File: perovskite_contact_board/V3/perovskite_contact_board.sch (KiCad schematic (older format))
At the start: 31 parts, among them U1 Perovskite_CP_6_Cell, U2 Perovskite_CP_6_Cell, U3 Perovskite_CP_6_Cell, U4 MCP9808_MSOP, U5 MCP9808_MSOP, U6 MCP9808_MSOP

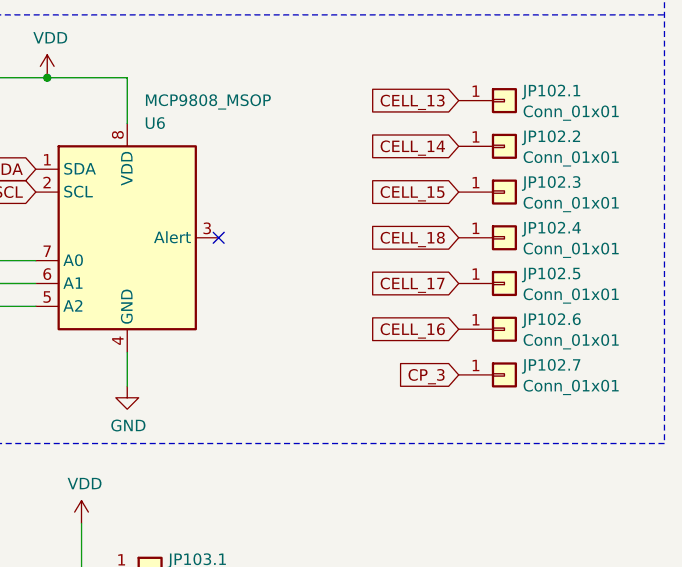
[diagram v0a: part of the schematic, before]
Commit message: Update ready for review
Swapped to circular 2mm touch point pads.
Updated 3d models.
Ready for review.
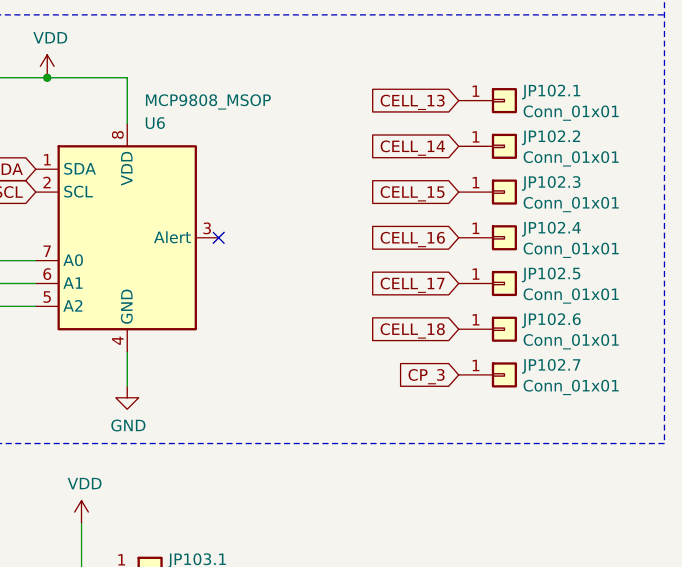
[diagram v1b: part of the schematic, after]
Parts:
- JP100.1, JP100.2, JP100.3, JP100.4, JP100.5, JP100.6, JP100.7, JP101.1, JP101.2, JP101.3, JP101.4, JP101.5, JP101.6, JP101.7, JP102.1, JP102.2, JP102.3, JP102.4, JP102.5, JP102.6, JP102.7, JP103.1, JP103.2, JP103.3, JP103.4: footprint TestPoint:TestPoint_Keystone_5015_Micro-Minature -> TestPoint:TestPoint_Pad_D2.0mm
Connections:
- net CELL_16: now also JP102.4.1 (Pin_1); no longer JP102.6.1 (Pin_1)
- net CELL_18: now also JP102.6.1 (Pin_1); no longer JP102.4.1 (Pin_1)
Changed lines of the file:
@@
 Text GLabel 7000 4050 0    50   Input ~ 0
 CELL_12
-Text GLabel 6950 5900 0    50   Input ~ 0
+Text GLabel 6950 5500 0    50   Input ~ 0
 CELL_16
 $Comp
@@
 F 0 "JP100.1" H 7280 1192 50  0000 L CNN
 F 1 "Conn_01x01" H 7280 1101 50  0000 L CNN
-F 2 "TestPoint:TestPoint_Keystone_5015_Micro-Minature" H 7200 1150 50  0001 C CNN
+F 2 "TestPoint:TestPoint_Pad_D2.0mm" H 7200 1150 50  0001 C CNN
 F 3 "~" H 7200 1150 50  0001 C CNN
 	1    7200 1150
@@
 F 0 "JP100.2" H 7280 1392 50  0000 L CNN
 F 1 "Conn_01x01" H 7280 1301 50  0000 L CNN
-F 2 "TestPoint:TestPoint_Keystone_5015_Micro-Minature" H 7200 1350 50  0001 C CNN
+F 2 "TestPoint:TestPoint_Pad_D2.0mm" H 7200 1350 50  0001 C CNN
 F 3 "~" H 7200 1350 50  0001 C CNN
 	1    7200 1350
@@
 F 0 "JP100.3" H 7280 1592 50  0000 L CNN
 F 1 "Conn_01x01" H 7280 1501 50  0000 L CNN
-F 2 "TestPoint:TestPoint_Keystone_5015_Micro-Minature" H 7200 1550 50  0001 C CNN
+F 2 "TestPoint:TestPoint_Pad_D2.0mm" H 7200 1550 50  0001 C CNN
 F 3 "~" H 7200 1550 50  0001 C CNN
 	1    7200 1550
@@
 F 0 "JP100.4" H 7280 1792 50  0000 L CNN
 F 1 "Conn_01x01" H 7280 1701 50  0000 L CNN
-F 2 "TestPoint:TestPoint_Keystone_5015_Micro-Minature" H 7200 1750 50  0001 C CNN
+F 2 "TestPoint:TestPoint_Pad_D2.0mm" H 7200 1750 50  0001 C CNN
 F 3 "~" H 7200 1750 50  0001 C CNN
 	1    7200 1750
@@
 F 0 "JP100.5" H 7280 1992 50  0000 L CNN
 F 1 "Conn_01x01" H 7280 1901 50  0000 L CNN
-F 2 "TestPoint:TestPoint_Keystone_5015_Micro-Minature" H 7200 1950 50  0001 C CNN
+F 2 "TestPoint:TestPoint_Pad_D2.0mm" H 7200 1950 50  0001 C CNN
 F 3 "~" H 7200 1950 50  0001 C CNN
 	1    7200 1950
@@
 F 0 "JP100.6" H 7280 2192 50  0000 L CNN
 F 1 "Conn_01x01" H 7280 2101 50  0000 L CNN
-F 2 "TestPoint:TestPoint_Keystone_5015_Micro-Minature" H 7200 2150 50  0001 C CNN
+F 2 "TestPoint:TestPoint_Pad_D2.0mm" H 7200 2150 50  0001 C CNN
 F 3 "~" H 7200 2150 50  0001 C CNN
 	1    7200 2150
@@
 F 0 "JP100.7" H 7280 2392 50  0000 L CNN
 F 1 "Conn_01x01" H 7280 2301 50  0000 L CNN
-F 2 "TestPoint:TestPoint_Keystone_5015_Micro-Minature" H 7200 2350 50  0001 C CNN
+F 2 "TestPoint:TestPoint_Pad_D2.0mm" H 7200 2350 50  0001 C CNN
 F 3 "~" H 7200 2350 50  0001 C CNN
 	1    7200 2350
@@
 F 0 "JP101.1" H 7280 3092 50  0000 L CNN
 F 1 "Conn_01x01" H 7280 3001 50  0000 L CNN
-F 2 "TestPoint:TestPoint_Keystone_5015_Micro-Minature" H 7200 3050 50  0001 C CNN
+F 2 "TestPoint:TestPoint_Pad_D2.0mm" H 7200 3050 50  0001 C CNN
 F 3 "~" H 7200 3050 50  0001 C CNN
 	1    7200 3050
@@
 F 0 "JP101.2" H 7280 3292 50  0000 L CNN
 F 1 "Conn_01x01" H 7280 3201 50  0000 L CNN
-F 2 "TestPoint:TestPoint_Keystone_5015_Micro-Minature" H 7200 3250 50  0001 C CNN
+F 2 "TestPoint:TestPoint_Pad_D2.0mm" H 7200 3250 50  0001 C CNN
 F 3 "~" H 7200 3250 50  0001 C CNN
 	1    7200 3250
@@
 F 0 "JP101.3" H 7280 3492 50  0000 L CNN
 F 1 "Conn_01x01" H 7280 3401 50  0000 L CNN
-F 2 "TestPoint:TestPoint_Keystone_5015_Micro-Minature" H 7200 3450 50  0001 C CNN
+F 2 "TestPoint:TestPoint_Pad_D2.0mm" H 7200 3450 50  0001 C CNN
 F 3 "~" H 7200 3450 50  0001 C CNN
 	1    7200 3450
@@
 F 0 "JP101.4" H 7280 3692 50  0000 L CNN
 F 1 "Conn_01x01" H 7280 3601 50  0000 L CNN
-F 2 "TestPoint:TestPoint_Keystone_5015_Micro-Minature" H 7200 3650 50  0001 C CNN
+F 2 "TestPoint:TestPoint_Pad_D2.0mm" H 7200 3650 50  0001 C CNN
 F 3 "~" H 7200 3650 50  0001 C CNN
 	1    7200 3650
@@
 F 0 "JP101.5" H 7280 3892 50  0000 L CNN
 F 1 "Conn_01x01" H 7280 3801 50  0000 L CNN
-F 2 "TestPoint:TestPoint_Keystone_5015_Micro-Minature" H 7200 3850 50  0001 C CNN
+F 2 "TestPoint:TestPoint_Pad_D2.0mm" H 7200 3850 50  0001 C CNN
 F 3 "~" H 7200 3850 50  0001 C CNN
 	1    7200 3850
@@
 F 0 "JP101.6" H 7280 4092 50  0000 L CNN
 F 1 "Conn_01x01" H 7280 4001 50  0000 L CNN
-F 2 "TestPoint:TestPoint_Keystone_5015_Micro-Minature" H 7200 4050 50  0001 C CNN
+F 2 "TestPoint:TestPoint_Pad_D2.0mm" H 7200 4050 50  0001 C CNN
 F 3 "~" H 7200 4050 50  0001 C CNN
 	1    7200 4050
@@
 F 0 "JP101.7" H 7280 4292 50  0000 L CNN
 F 1 "Conn_01x01" H 7280 4201 50  0000 L CNN
-F 2 "TestPoint:TestPoint_Keystone_5015_Micro-Minature" H 7200 4250 50  0001 C CNN
+F 2 "TestPoint:TestPoint_Pad_D2.0mm" H 7200 4250 50  0001 C CNN
 F 3 "~" H 7200 4250 50  0001 C CNN
 	1    7200 4250
@@
 F 0 "JP102.1" H 7230 4942 50  0000 L CNN
 F 1 "Conn_01x01" H 7230 4851 50  0000 L CNN
-F 2 "TestPoint:TestPoint_Keystone_5015_Micro-Minature" H 7150 4900 50  0001 C CNN
+F 2 "TestPoint:TestPoint_Pad_D2.0mm" H 7150 4900 50  0001 C CNN
 F 3 "~" H 7150 4900 50  0001 C CNN
 	1    7150 4900
@@
 F 0 "JP102.2" H 7230 5142 50  0000 L CNN
 F 1 "Conn_01x01" H 7230 5051 50  0000 L CNN
-F 2 "TestPoint:TestPoint_Keystone_5015_Micro-Minature" H 7150 5100 50  0001 C CNN
+F 2 "TestPoint:TestPoint_Pad_D2.0mm" H 7150 5100 50  0001 C CNN
 F 3 "~" H 7150 5100 50  0001 C CNN
 	1    7150 5100
@@
 F 0 "JP102.3" H 7230 5342 50  0000 L CNN
 F 1 "Conn_01x01" H 7230 5251 50  0000 L CNN
-F 2 "TestPoint:TestPoint_Keystone_5015_Micro-Minature" H 7150 5300 50  0001 C CNN
+F 2 "TestPoint:TestPoint_Pad_D2.0mm" H 7150 5300 50  0001 C CNN
 F 3 "~" H 7150 5300 50  0001 C CNN
 	1    7150 5300
@@
 F 0 "JP102.4" H 7230 5542 50  0000 L CNN
 F 1 "Conn_01x01" H 7230 5451 50  0000 L CNN
-F 2 "TestPoint:TestPoint_Keystone_5015_Micro-Minature" H 7150 5500 50  0001 C CNN
+F 2 "TestPoint:TestPoint_Pad_D2.0mm" H 7150 5500 50  0001 C CNN
 F 3 "~" H 7150 5500 50  0001 C CNN
 	1    7150 5500
@@
 F 0 "JP102.5" H 7230 5742 50  0000 L CNN
 F 1 "Conn_01x01" H 7230 5651 50  0000 L CNN
-F 2 "TestPoint:TestPoint_Keystone_5015_Micro-Minature" H 7150 5700 50  0001 C CNN
+F 2 "TestPoint:TestPoint_Pad_D2.0mm" H 7150 5700 50  0001 C CNN
 F 3 "~" H 7150 5700 50  0001 C CNN
 	1    7150 5700
@@
 F 0 "JP102.6" H 7230 5942 50  0000 L CNN
 F 1 "Conn_01x01" H 7230 5851 50  0000 L CNN
-F 2 "TestPoint:TestPoint_Keystone_5015_Micro-Minature" H 7150 5900 50  0001 C CNN
+F 2 "TestPoint:TestPoint_Pad_D2.0mm" H 7150 5900 50  0001 C CNN
 F 3 "~" H 7150 5900 50  0001 C CNN
 	1    7150 5900
@@
 F 0 "JP102.7" H 7230 6142 50  0000 L CNN
 F 1 "Conn_01x01" H 7230 6051 50  0000 L CNN
-F 2 "TestPoint:TestPoint_Keystone_5015_Micro-Minature" H 7150 6100 50  0001 C CNN
+F 2 "TestPoint:TestPoint_Pad_D2.0mm" H 7150 6100 50  0001 C CNN
 F 3 "~" H 7150 6100 50  0001 C CNN
 	1    7150 6100
@@
 F 0 "JP103.1" H 5680 6992 50  0000 L CNN
 F 1 "Conn_01x01" H 5680 6901 50  0000 L CNN
-F 2 "TestPoint:TestPoint_Keystone_5015_Micro-Minature" H 5600 6950 50  0001 C CNN
+F 2 "TestPoint:TestPoint_Pad_D2.0mm" H 5600 6950 50  0001 C CNN
 F 3 "~" H 5600 6950 50  0001 C CNN
 	1    5600 6950
@@
 F 0 "JP103.2" H 5680 7192 50  0000 L CNN
 F 1 "Conn_01x01" H 5680 7101 50  0000 L CNN
-F 2 "TestPoint:TestPoint_Keystone_5015_Micro-Minature" H 5600 7150 50  0001 C CNN
+F 2 "TestPoint:TestPoint_Pad_D2.0mm" H 5600 7150 50  0001 C CNN
 F 3 "~" H 5600 7150 50  0001 C CNN
 	1    5600 7150
@@
 F 0 "JP103.3" H 5680 7392 50  0000 L CNN
 F 1 "Conn_01x01" H 5680 7301 50  0000 L CNN
-F 2 "TestPoint:TestPoint_Keystone_5015_Micro-Minature" H 5600 7350 50  0001 C CNN
+F 2 "TestPoint:TestPoint_Pad_D2.0mm" H 5600 7350 50  0001 C CNN
 F 3 "~" H 5600 7350 50  0001 C CNN
 	1    5600 7350
@@
 F 0 "JP103.4" H 5680 7592 50  0000 L CNN
 F 1 "Conn_01x01" H 5680 7501 50  0000 L CNN
-F 2 "TestPoint:TestPoint_Keystone_5015_Micro-Minature" H 5600 7550 50  0001 C CNN
+F 2 "TestPoint:TestPoint_Pad_D2.0mm" H 5600 7550 50  0001 C CNN
 F 3 "~" H 5600 7550 50  0001 C CNN
 	1    5600 7550
@@
 $EndComp
 $Comp
-L power:GND #PWR?
+L power:GND #PWR0102
 U 1 1 64BAB42F
 P 5050 7300
-F 0 "#PWR?" H 5050 7050 50  0001 C CNN
+F 0 "#PWR0102" H 5050 7050 50  0001 C CNN
 F 1 "GND" H 5055 7127 50  0000 C CNN
 F 2 "" H 5050 7300 50  0001 C CNN
@@
 	5050 6950 5050 7300
 $Comp
-L power:VDD #PWR?
+L power:VDD #PWR0103
 U 1 1 64BB3055
 P 5300 6750
-F 0 "#PWR?" H 5300 6600 50  0001 C CNN
+F 0 "#PWR0103" H 5300 6600 50  0001 C CNN
 F 1 "VDD" H 5315 6923 50  0000 C CNN
 F 2 "" H 5300 6750 50  0001 C CNN
@@
 	7850 2675 975  2675
 $Comp
-L power:VDD #PWR?
+L power:VDD #PWR0105
 U 1 1 64BC9726
 P 5150 4800
-F 0 "#PWR?" H 5150 4650 50  0001 C CNN
+F 0 "#PWR0105" H 5150 4650 50  0001 C CNN
 F 1 "VDD" H 5165 4973 50  0000 C CNN
 F 2 "" H 5150 4800 50  0001 C CNN
@@
 	5150 4800 4800 4800
 $Comp
-L power:VDD #PWR?
+L power:VDD #PWR0106
 U 1 1 64BCA3BE
 P 5150 2950
-F 0 "#PWR?" H 5150 2800 50  0001 C CNN
+F 0 "#PWR0106" H 5150 2800 50  0001 C CNN
 F 1 "VDD" H 5165 3123 50  0000 C CNN
 F 2 "" H 5150 2950 50  0001 C CNN
@@
 	5150 2950 4750 2950
 $Comp
-L power:VDD #PWR?
+L power:VDD #PWR0107
 U 1 1 64BCB08F
 P 5150 1200
-F 0 "#PWR?" H 5150 1050 50  0001 C CNN
+F 0 "#PWR0107" H 5150 1050 50  0001 C CNN
 F 1 "VDD" H 5165 1373 50  0000 C CNN
 F 2 "" H 5150 1200 50  0001 C CNN
@@
 Wire Wire Line
 	5150 1200 4800 1200
-Text GLabel 6950 5500 0    50   Input ~ 0
+Text GLabel 6950 5900 0    50   Input ~ 0
 CELL_18
 Text GLabel 6950 5700 0    50   Input ~ 0

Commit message: Review contact board
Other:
- moved on the sheet: JP100.1, JP100.2, JP100.3, JP100.4, JP100.5, JP100.6, JP100.7, JP101.1, JP101.2, JP101.3, JP101.4, JP101.5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

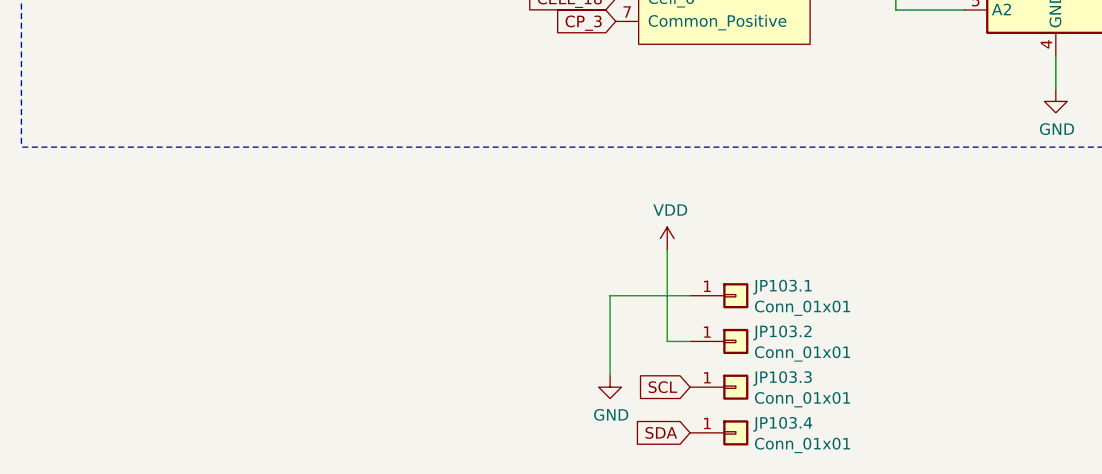
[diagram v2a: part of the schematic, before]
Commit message: centered vias, added all redundant pads, standardized text
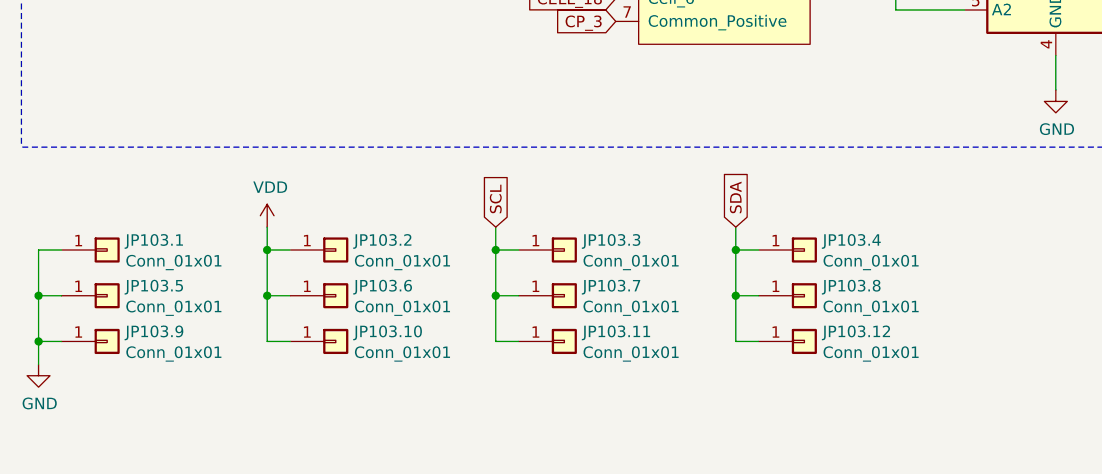
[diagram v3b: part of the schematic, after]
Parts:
- added JP103.10, JP103.11, JP103.12, JP103.5, JP103.6, JP103.7, JP103.8, JP103.9: Conn_01x01, TestPoint:TestPoint_Pad_D2.0mm, symbol Connector_Generic:Conn_01x01
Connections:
- net GND: now also JP103.5.1 (Pin_1), JP103.9.1 (Pin_1)
- net SCL: now also JP103.11.1 (Pin_1), JP103.7.1 (Pin_1)
- net SDA: now also JP103.12.1 (Pin_1), JP103.8.1 (Pin_1)
- net VDD: now also JP103.10.1 (Pin_1), JP103.6.1 (Pin_1)
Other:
- moved on the sheet: JP103.1, JP103.2, JP103.3, JP103.4
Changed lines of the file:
@@
 Sheet 1 1
 Title "Perovskite Contact Board"
-Date "2022-11-26"
-Rev "Version 1"
+Date "2023-07-20"
+Rev "V3"
 Comp "Aerospace eXperimental Payloads | UNL Aerospace Club"
 Comment1 "Copyright (c) 2022"
@@
 L Connector_Generic:Conn_01x01 JP103.1
 U 1 1 64B5D0FC
-P 5600 6950
-F 0 "JP103.1" H 5680 6992 50  0000 L CNN
-F 1 "Conn_01x01" H 5680 6901 50  0000 L CNN
-F 2 "TestPoint:TestPoint_Pad_D2.0mm" H 5600 6950 50  0001 C CNN
-F 3 "~" H 5600 6950 50  0001 C CNN
-	1    5600 6950
+P 2850 6750
+F 0 "JP103.1" H 2930 6792 50  0000 L CNN
+F 1 "Conn_01x01" H 2930 6701 50  0000 L CNN
+F 2 "TestPoint:TestPoint_Pad_D2.0mm" H 2850 6750 50  0001 C CNN
+F 3 "~" H 2850 6750 50  0001 C CNN
+	1    2850 6750
 	1    0    0    -1
 $EndComp
@@
 L Connector_Generic:Conn_01x01 JP103.2
 U 1 1 64B5D102
-P 5600 7150
-F 0 "JP103.2" H 5680 7192 50  0000 L CNN
-F 1 "Conn_01x01" H 5680 7101 50  0000 L CNN
-F 2 "TestPoint:TestPoint_Pad_D2.0mm" H 5600 7150 50  0001 C CNN
-F 3 "~" H 5600 7150 50  0001 C CNN
-	1    5600 7150
+P 3850 6750
+F 0 "JP103.2" H 3930 6792 50  0000 L CNN
+F 1 "Conn_01x01" H 3930 6701 50  0000 L CNN
+F 2 "TestPoint:TestPoint_Pad_D2.0mm" H 3850 6750 50  0001 C CNN
+F 3 "~" H 3850 6750 50  0001 C CNN
+	1    3850 6750
 	1    0    0    -1
 $EndComp
@@
 L Connector_Generic:Conn_01x01 JP103.3
 U 1 1 64B5D108
-P 5600 7350
-F 0 "JP103.3" H 5680 7392 50  0000 L CNN
-F 1 "Conn_01x01" H 5680 7301 50  0000 L CNN
-F 2 "TestPoint:TestPoint_Pad_D2.0mm" H 5600 7350 50  0001 C CNN
-F 3 "~" H 5600 7350 50  0001 C CNN
-	1    5600 7350
+P 4850 6750
+F 0 "JP103.3" H 4930 6792 50  0000 L CNN
+F 1 "Conn_01x01" H 4930 6701 50  0000 L CNN
+F 2 "TestPoint:TestPoint_Pad_D2.0mm" H 4850 6750 50  0001 C CNN
+F 3 "~" H 4850 6750 50  0001 C CNN
+	1    4850 6750
 	1    0    0    -1
 $EndComp
@@
 L Connector_Generic:Conn_01x01 JP103.4
 U 1 1 64B7D4E1
-P 5600 7550
-F 0 "JP103.4" H 5680 7592 50  0000 L CNN
-F 1 "Conn_01x01" H 5680 7501 50  0000 L CNN
-F 2 "TestPoint:TestPoint_Pad_D2.0mm" H 5600 7550 50  0001 C CNN
-F 3 "~" H 5600 7550 50  0001 C CNN
-	1    5600 7550
+P 5900 6750
+F 0 "JP103.4" H 5980 6792 50  0000 L CNN
+F 1 "Conn_01x01" H 5980 6701 50  0000 L CNN
+F 2 "TestPoint:TestPoint_Pad_D2.0mm" H 5900 6750 50  0001 C CNN
+F 3 "~" H 5900 6750 50  0001 C CNN
+	1    5900 6750
 	1    0    0    -1
 $EndComp
@@
 L power:GND #PWR0102
 U 1 1 64BAB42F
-P 5050 7300
-F 0 "#PWR0102" H 5050 7050 50  0001 C CNN
-F 1 "GND" H 5055 7127 50  0000 C CNN
-F 2 "" H 5050 7300 50  0001 C CNN
-F 3 "" H 5050 7300 50  0001 C CNN
-	1    5050 7300
-	1    0    0    -1
-$EndComp
-Text GLabel 5400 7550 0    50   Input ~ 0
+P 2550 7250
+F 0 "#PWR0102" H 2550 7000 50  0001 C CNN
+F 1 "GND" H 2555 7077 50  0000 C CNN
+F 2 "" H 2550 7250 50  0001 C CNN
+F 3 "" H 2550 7250 50  0001 C CNN
+	1    2550 7250
+	1    0    0    -1
+$EndComp
+Text GLabel 5600 6650 1    50   Input ~ 0
 SDA
-Text GLabel 5400 7350 0    50   Input ~ 0
+Text GLabel 4550 6650 1    50   Input ~ 0
 SCL
-Wire Wire Line
-	5400 6950 5050 6950
-Wire Wire Line
-	5050 6950 5050 7300
 $Comp
 L power:VDD #PWR0103
 U 1 1 64BB3055
-P 5300 6750
-F 0 "#PWR0103" H 5300 6600 50  0001 C CNN
-F 1 "VDD" H 5315 6923 50  0000 C CNN
-F 2 "" H 5300 6750 50  0001 C CNN
-F 3 "" H 5300 6750 50  0001 C CNN
-	1    5300 6750
-	1    0    0    -1
-$EndComp
-Wire Wire Line
-	5400 7150 5300 7150
-Wire Wire Line
-	5300 7150 5300 6750
+P 3550 6650
+F 0 "#PWR0103" H 3550 6500 50  0001 C CNN
+F 1 "VDD" H 3565 6823 50  0000 C CNN
+F 2 "" H 3550 6650 50  0001 C CNN
+F 3 "" H 3550 6650 50  0001 C CNN
+	1    3550 6650
+	1    0    0    -1
+$EndComp
 NoConn ~ 7400 5400
 NoConn ~ 7400 3550
@@
 Text GLabel 8500 2250 0    50   Input ~ 0
 CP_1
+$Comp
+L Connector_Generic:Conn_01x01 JP103.5
+U 1 1 64B97803
+P 2850 6950
+F 0 "JP103.5" H 2930 6992 50  0000 L CNN
+F 1 "Conn_01x01" H 2930 6901 50  0000 L CNN
+F 2 "TestPoint:TestPoint_Pad_D2.0mm" H 2850 6950 50  0001 C CNN
+F 3 "~" H 2850 6950 50  0001 C CNN
+	1    2850 6950
+	1    0    0    -1
+$EndComp
+$Comp
+L Connector_Generic:Conn_01x01 JP103.9
+U 1 1 64B97AC2
+P 2850 7150
+F 0 "JP103.9" H 2930 7192 50  0000 L CNN
+F 1 "Conn_01x01" H 2930 7101 50  0000 L CNN
+F 2 "TestPoint:TestPoint_Pad_D2.0mm" H 2850 7150 50  0001 C CNN
+F 3 "~" H 2850 7150 50  0001 C CNN
+	1    2850 7150
+	1    0    0    -1
+$EndComp
+$Comp
+L Connector_Generic:Conn_01x01 JP103.6
+U 1 1 64B9861B
+P 3850 6950
+F 0 "JP103.6" H 3930 6992 50  0000 L CNN
+F 1 "Conn_01x01" H 3930 6901 50  0000 L CNN
+F 2 "TestPoint:TestPoint_Pad_D2.0mm" H 3850 6950 50  0001 C CNN
+F 3 "~" H 3850 6950 50  0001 C CNN
+	1    3850 6950
+	1    0    0    -1
+$EndComp
+$Comp
+L Connector_Generic:Conn_01x01 JP103.10
+U 1 1 64B988DA
+P 3850 7150
+F 0 "JP103.10" H 3930 7192 50  0000 L CNN
+F 1 "Conn_01x01" H 3930 7101 50  0000 L CNN
+F 2 "TestPoint:TestPoint_Pad_D2.0mm" H 3850 7150 50  0001 C CNN
+F 3 "~" H 3850 7150 50  0001 C CNN
+	1    3850 7150
+	1    0    0    -1
+$EndComp
+Wire Wire Line
+	3650 7150 3550 7150
+Wire Wire Line
+	3550 7150 3550 6950
+Wire Wire Line
+	3650 6750 3550 6750
+Connection ~ 3550 6750
+Wire Wire Line
+	3550 6750 3550 6650
+Wire Wire Line
+	3650 6950 3550 6950
+Connection ~ 3550 6950
+Wire Wire Line
+	3550 6950 3550 6750
+Wire Wire Line
+	2550 7250 2550 7150
+Wire Wire Line
+	2550 6750 2650 6750
+Wire Wire Line
+	2650 6950 2550 6950
+Connection ~ 2550 6950
+Wire Wire Line
+	2550 6950 2550 6750
+Wire Wire Line
+	2650 7150 2550 7150
+Connection ~ 2550 7150
+Wire Wire Line
+	2550 7150 2550 6950
+$Comp
+L Connector_Generic:Conn_01x01 JP103.7
+U 1 1 64BA556D
+P 4850 6950
+F 0 "JP103.7" H 4930 6992 50  0000 L CNN
+F 1 "Conn_01x01" H 4930 6901 50  0000 L CNN
+F 2 "TestPoint:TestPoint_Pad_D2.0mm" H 4850 6950 50  0001 C CNN
+F 3 "~" H 4850 6950 50  0001 C CNN
+	1    4850 6950
+	1    0    0    -1
+$EndComp
+$Comp
+L Connector_Generic:Conn_01x01 JP103.11
+U 1 1 64BA5848
+P 4850 7150
+F 0 "JP103.11" H 4930 7192 50  0000 L CNN
+F 1 "Conn_01x01" H 4930 7101 50  0000 L CNN
+F 2 "TestPoint:TestPoint_Pad_D2.0mm" H 4850 7150 50  0001 C CNN
+F 3 "~" H 4850 7150 50  0001 C CNN
+	1    4850 7150
+	1    0    0    -1
+$EndComp
+$Comp
+L Connector_Generic:Conn_01x01 JP103.8
+U 1 1 64BA5C01
+P 5900 6950
+F 0 "JP103.8" H 5980 6992 50  0000 L CNN
+F 1 "Conn_01x01" H 5980 6901 50  0000 L CNN
+F 2 "TestPoint:TestPoint_Pad_D2.0mm" H 5900 6950 50  0001 C CNN
+F 3 "~" H 5900 6950 50  0001 C CNN
+	1    5900 6950
+	1    0    0    -1
+$EndComp
+$Comp
+L Connector_Generic:Conn_01x01 JP103.12
+U 1 1 64BA5ED3
+P 5900 7150
+F 0 "JP103.12" H 5980 7192 50  0000 L CNN
+F 1 "Conn_01x01" H 5980 7101 50  0000 L CNN
+F 2 "TestPoint:TestPoint_Pad_D2.0mm" H 5900 7150 50  0001 C CNN
+F 3 "~" H 5900 7150 50  0001 C CNN
+	1    5900 7150
+	1    0    0    -1
+$EndComp
+Wire Wire Line
+	4550 6650 4550 6750
+Wire Wire Line
+	4550 7150 4650 7150
+Wire Wire Line
+	4650 6750 4550 6750
+Connection ~ 4550 6750
+Wire Wire Line
+	4550 6750 4550 6950
+Wire Wire Line
+	4650 6950 4550 6950
+Connection ~ 4550 6950
+Wire Wire Line
+	4550 6950 4550 7150
+Wire Wire Line
+	5600 6650 5600 6750
+Wire Wire Line
+	5600 7150 5700 7150
+Wire Wire Line
+	5700 6950 5600 6950
+Connection ~ 5600 6950
+Wire Wire Line
+	5600 6950 5600 7150
+Wire Wire Line
+	5700 6750 5600 6750
+Connection ~ 5600 6750
+Wire Wire Line
+	5600 6750 5600 6950
 $EndSCHEMATC
